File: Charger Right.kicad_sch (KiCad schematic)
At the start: 6 parts, among them Q3 AO4459, U2 CN3702

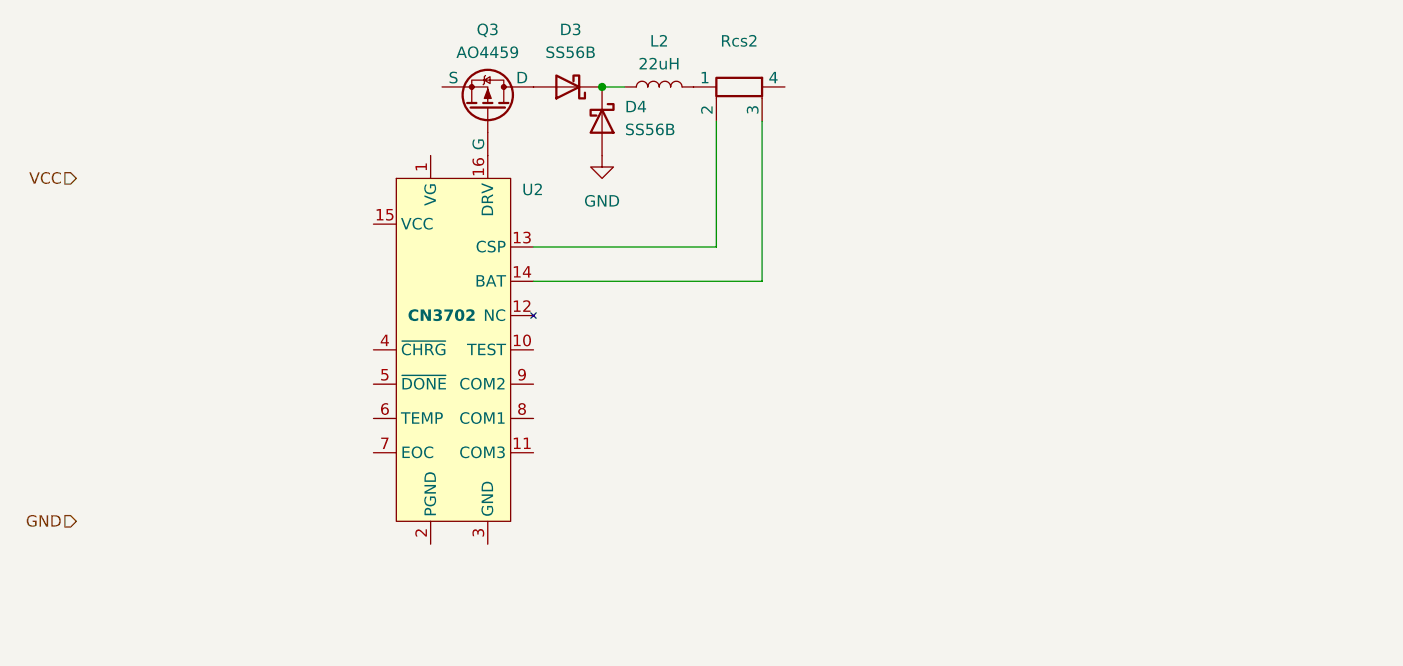
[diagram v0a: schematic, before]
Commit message: Add some resistors and caps
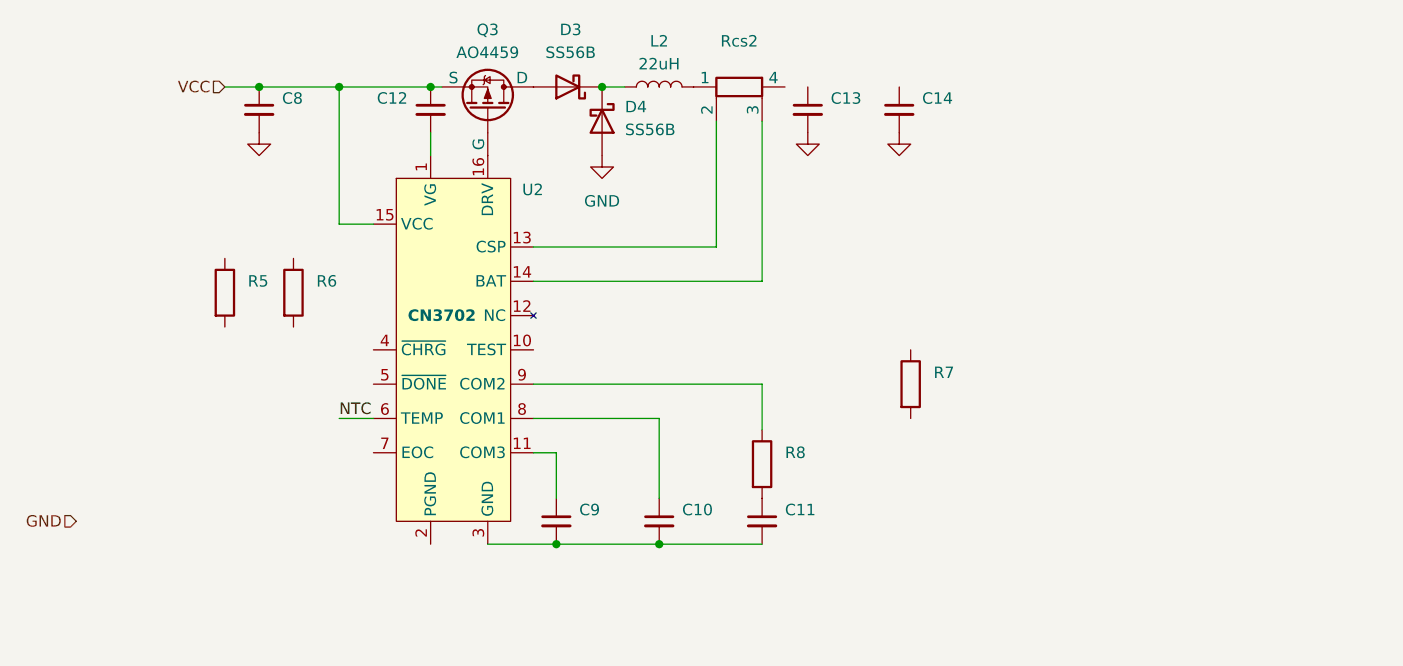
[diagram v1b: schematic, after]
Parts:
- added C10, C11, C12, C13, C14, C8, C9: (no value), symbol Device:C_Small
- added R5, R6, R7, R8: (no value), symbol Device:R
- Rcs2: footprint (none) -> BRAUNIT Charger:R_Shunt_2010_5025Metric
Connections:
- net GND: now also C13.2, C14.2, C8.2
- net VCC: now also Q3.1 (S), Q3.2 (S), Q3.3 (S), U2.15 (VCC), C12.1, C8.1
- net at U2.1 (VG): now also C12.2
- net at U2.11 (COM3): now also C9.1
- net at U2.3 (GND): now also C10.2, C11.2, C9.2
- net NTC: now reaches U2.6 (TEMP)
- net at U2.8 (COM1): now also C10.1
- net at U2.9 (COM2): now also R8.1
- new net: C11.1, R8.2

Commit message: Add BRAUNIT connector and battery detect/charge enable
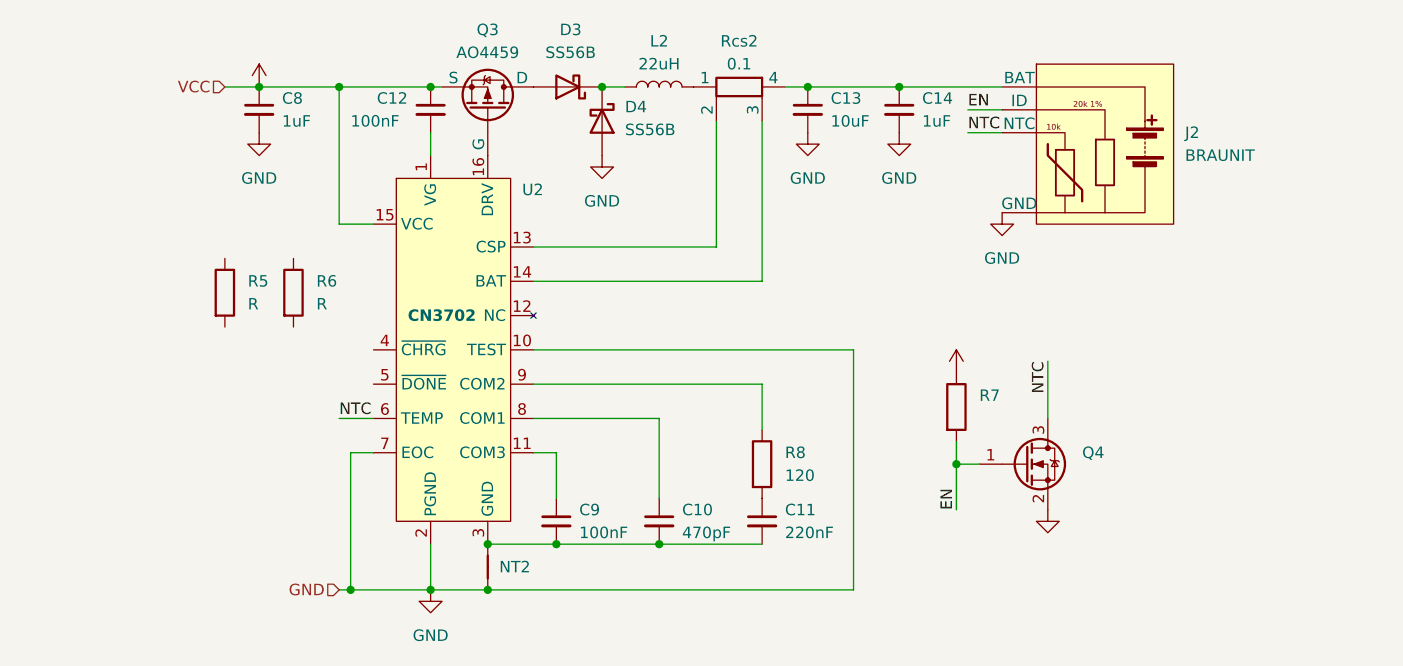
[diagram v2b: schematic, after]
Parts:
- added J2: BRAUNIT, BRAUNIT Charger:Blade_1x04_P2.5mm_Vertical_BRAUNIT_Loose, symbol BRAUNIT Charger:BRAUNIT
- added NT2: NetTie_2, NetTie:NetTie-2_SMD_Pad0.5mm, symbol Device:NetTie_2
- added Q4: (no value), symbol Transistor_FET:2N7002
- C10: value (none) -> 470pF; footprint (none) -> Capacitor_SMD:C_0805_2012Metric
- C11: value (none) -> 220nF; footprint (none) -> Capacitor_SMD:C_0805_2012Metric
- C12, C9: value (none) -> 100nF; footprint (none) -> Capacitor_SMD:C_0805_2012Metric
- C13: value (none) -> 10uF; footprint (none) -> Capacitor_SMD:C_1206_3216Metric
- C14, C8: value (none) -> 1uF; footprint (none) -> Capacitor_SMD:C_0805_2012Metric
- R5, R6: value (none) -> R
- R8: value (none) -> 120; footprint (none) -> Resistor_SMD:R_0805_2012Metric
- Rcs2: value (none) -> 0.1
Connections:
- net GND: now also U2.10 (TEST), U2.2 (PGND), U2.7 (EOC), J2.4 (GND), NT2.2, Q4.2 (S)
- net NTC: now also J2.3 (NTC), Q4.3 (D)
- net VCC: now also R7.1
- net at C10.2, C11.2, C9.2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: now also NT2.1
- net at C13.1: now also C14.1, Rcs2.4, J2.1 (BAT)
- net EN: now reaches R7.2
- net EN: now also J2.2 (ID), Q4.1 (G)
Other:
- moved on the sheet: R7

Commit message: Add LCSC part numbers for most components
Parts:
- removed D3, D4: SS56B, Diode_SMD:D_SMB, symbol BRAUNIT Charger:SS56B
- added D4, D5: (no value), symbol Device:D_Schottky
- added D6: LED_RAGB, symbol Device:LED_RAGB
- C10: value 470pF -> (none); footprint Capacitor_SMD:C_0805_2012Metric -> (none); LCSC (none) -> C107092
- C11: value 220nF -> (none); footprint Capacitor_SMD:C_0805_2012Metric -> (none); LCSC (none) -> C107131
- C12, C9: value 100nF -> (none); footprint Capacitor_SMD:C_0805_2012Metric -> (none); LCSC (none) -> C49678
- C13: value 10uF -> (none); footprint Capacitor_SMD:C_1206_3216Metric -> (none); LCSC (none) -> C109464
- C14, C8: value 1uF -> (none); footprint Capacitor_SMD:C_0805_2012Metric -> (none); LCSC (none) -> C91185
- J2: value BRAUNIT -> (none); footprint BRAUNIT Charger:Blade_1x04_P2.5mm_Vertical_BRAUNIT_Loose -> (none); now left out of the parts list
- L2: value 22uH -> (none); footprint Inductor_SMD:L_10.4x10.4_H4.8 -> (none); LCSC (none) -> C182173
- NT2: value NetTie_2 -> (none); footprint NetTie:NetTie-2_SMD_Pad0.5mm -> (none); now left out of the parts list
- Q3: value AO4459 -> (none); footprint Package_SO:SOIC-8_3.9x4.9mm_P1.27mm -> (none); LCSC (none) -> C49047
- Q4: LCSC (none) -> C8545
- R5: value R -> (none)
- R7: LCSC (none) -> C89104
- R8: value 120 -> (none); footprint Resistor_SMD:R_0805_2012Metric -> (none); LCSC (none) -> C114245
- Rcs2: value 0.1 -> (none); footprint BRAUNIT Charger:R_Shunt_2010_5025Metric -> (none); LCSC (none) -> C309644
- U2: value CN3702 -> (none); footprint Package_SO:TSSOP-16_4.4x5mm_P0.65mm -> (none); LCSC (none) -> C40655
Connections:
- net GND: now also D5.2 (A)
- net VCC: now also D6.2 (A)
- net at U2.4 (~{CHRG}): now also R5.2
- net at U2.5 (~{DONE}): now also R6.2
- net at L2.1: now also D4.1 (K), D5.1 (K)
- net at Q3.5 (D), Q3.6 (D), Q3.7 (D)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: now also D4.2 (A)
- net at R5.1: now also D6.1 (RK)
- net at R6.1: now also D6.3 (GK)
- no-connect marks 0 -> 1
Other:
- moved on the sheet: R5, R6

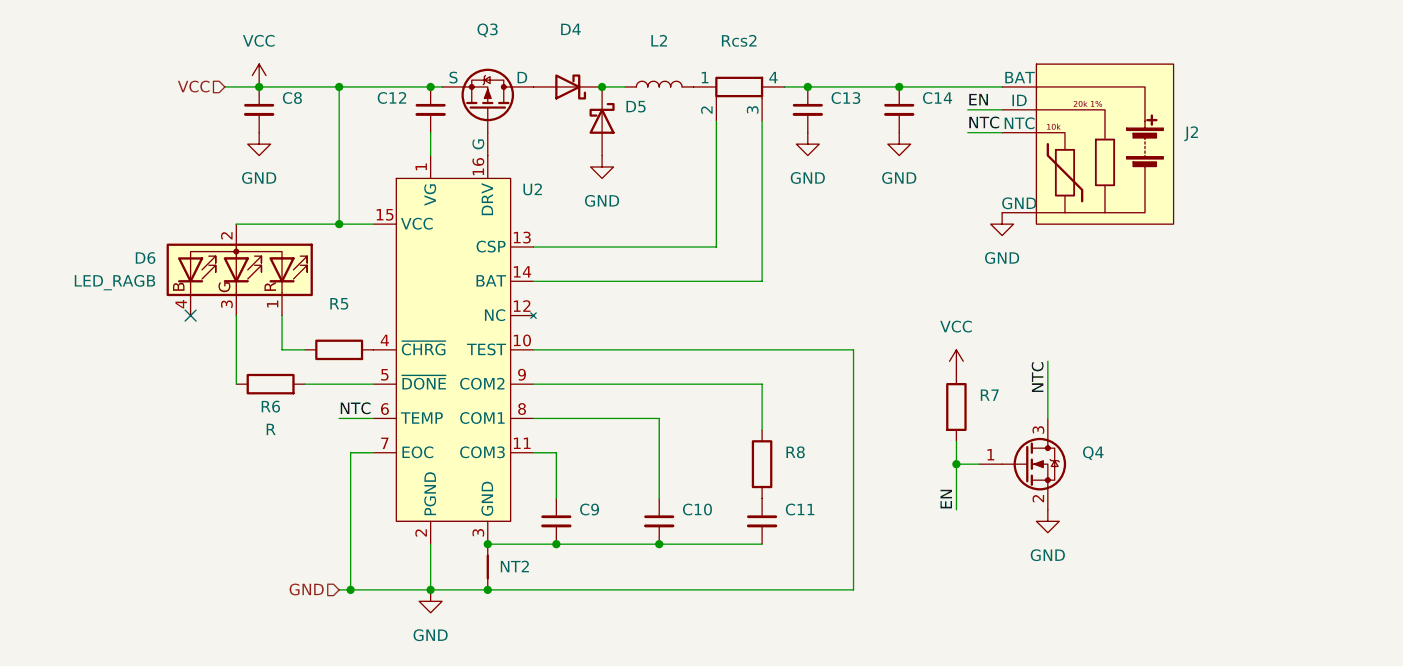
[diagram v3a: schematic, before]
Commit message: Add status indicator LED
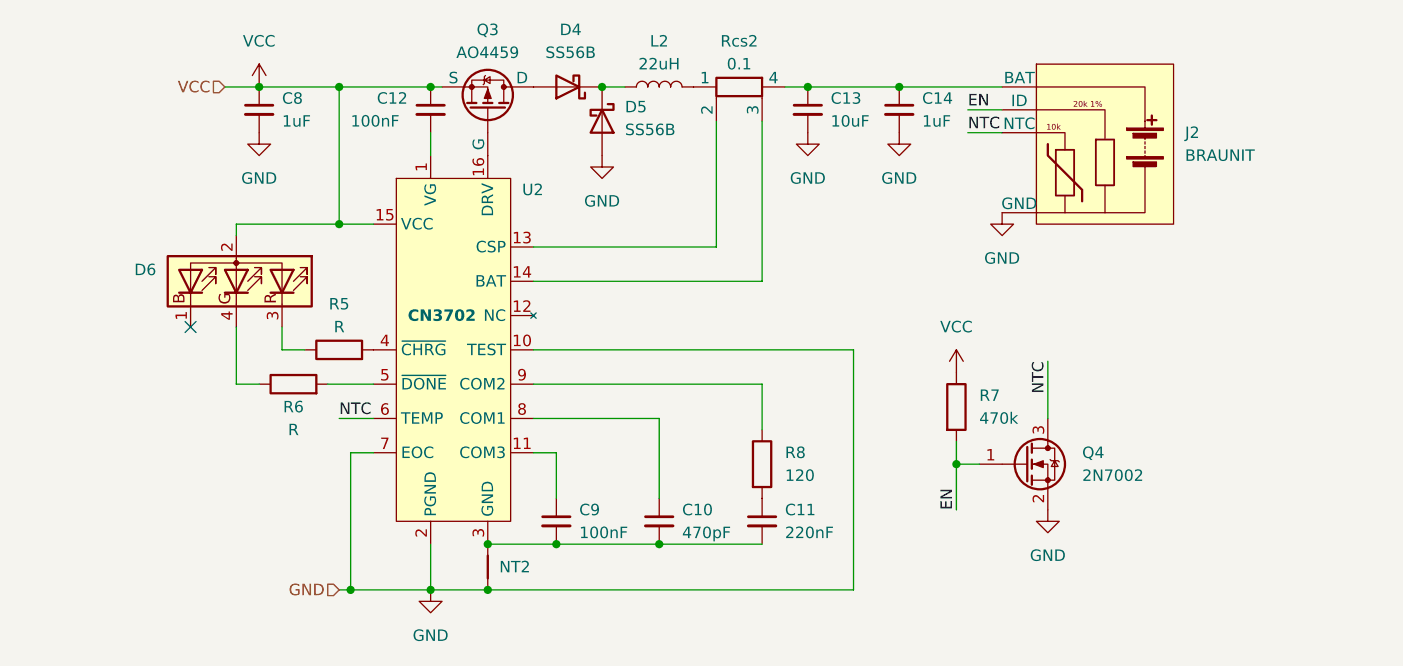
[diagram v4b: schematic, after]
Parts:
- removed D6: LED_RAGB, symbol Device:LED_RAGB
- added D6: (no value), symbol Device:LED_BARG
- C10: value (none) -> 470pF; footprint (none) -> Capacitor_SMD:C_0603_1608Metric
- C11: value (none) -> 220nF; footprint (none) -> Capacitor_SMD:C_0805_2012Metric
- C12, C9: value (none) -> 100nF; footprint (none) -> Capacitor_SMD:C_0805_2012Metric
- C13: value (none) -> 10uF; footprint (none) -> Capacitor_SMD:C_1206_3216Metric
- C14, C8: value (none) -> 1uF; footprint (none) -> Capacitor_SMD:C_0805_2012Metric
- D4, D5: value (none) -> SS56B; footprint (none) -> Diode_SMD:D_SMB
- J2: value (none) -> BRAUNIT; footprint (none) -> BRAUNIT Charger:Blade_1x04_P2.5mm_Vertical_BRAUNIT_Loose
- L2: value (none) -> 22uH; footprint (none) -> Inductor_SMD:L_10.4x10.4_H4.8
- NT2: value (none) -> NetTie_2; footprint (none) -> NetTie:NetTie-2_SMD_Pad0.5mm
- Q3: value (none) -> AO4459; footprint (none) -> Package_SO:SOIC-8_3.9x4.9mm_P1.27mm
- Q4: value (none) -> 2N7002; footprint (none) -> Package_TO_SOT_SMD:SOT-23
- R5: value (none) -> R
- R7: value (none) -> 470k; footprint (none) -> Resistor_SMD:R_0805_2012Metric
- R8: value (none) -> 120; footprint (none) -> Resistor_SMD:R_0805_2012Metric
- Rcs2: value (none) -> 0.1; footprint (none) -> BRAUNIT Charger:R_Shunt_2010_5025Metric
- U2: value (none) -> CN3702; footprint (none) -> Package_SO:TSSOP-16_4.4x5mm_P0.65mm
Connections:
- net VCC: now also D6.2 (A)
- net at R5.1: now also D6.3 (RK)
- net at R6.1: now also D6.4 (GK)
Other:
- moved on the sheet: R6

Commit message: Specify LED, resistors, and start on USB-C circuit
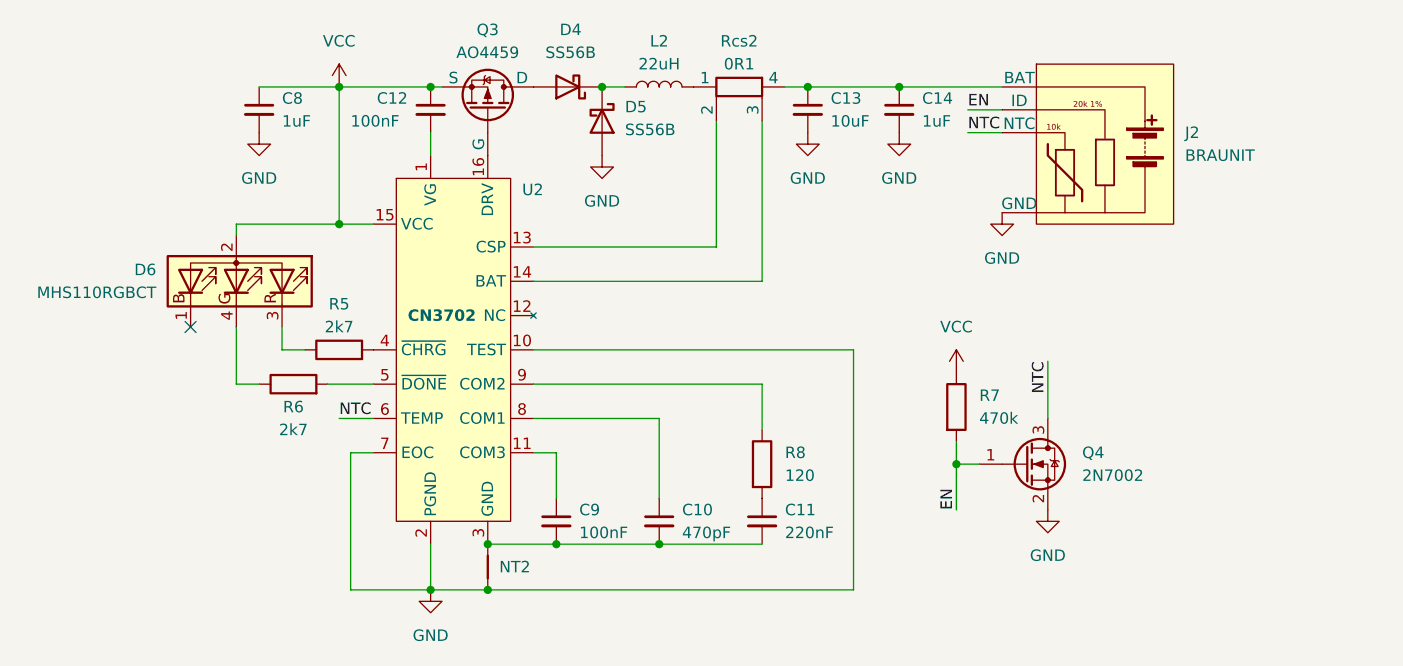
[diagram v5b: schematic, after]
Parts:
- D6: value (none) -> MHS110RGBCT; footprint (none) -> BRAUNIT Charger:LED_RGB_Meihua_MHS110RGBCT
- R5, R6: value R -> 2k7; footprint (none) -> Resistor_SMD:R_0603_1608Metric; LCSC (none) -> C114612
- Rcs2: value 0.1 -> 0R1
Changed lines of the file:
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@@
   (junction (at 138.43 123.19) (diameter 0) (color 0 0 0 0)
   )
-  (junction (at 115.57 128.27) (diameter 0) (color 0 0 0 0)
-  )
   (junction (at 114.3 72.39) (diameter 0) (color 0 0 0 0)
   )
@@
   )
   (junction (at 130.81 123.19) (diameter 0) (color 0 0 0 0)
-  )
-  (junction (at 105.41 72.39) (diameter 0) (color 0 0 0 0)
   )
   (junction (at 143.51 72.39) (diameter 0) (color 0 0 0 0)
@@
     (stroke (width 0) (type default) (color 0 0 0 0))
   )
-  (wire (pts (xy 101.6 72.39) (xy 105.41 72.39))
-    (stroke (width 0) (type default) (color 0 0 0 0))
-  )
   (wire (pts (xy 135.89 101.6) (xy 171.45 101.6))
     (stroke (width 0) (type default) (color 0 0 0 0))
@@
   )
   (wire (pts (xy 149.86 123.19) (xy 161.29 123.19))
-    (stroke (width 0) (type default) (color 0 0 0 0))
-  )
-  (wire (pts (xy 114.3 128.27) (xy 115.57 128.27))
     (stroke (width 0) (type default) (color 0 0 0 0))
   )
@@
   (label "NTC" (at 184.15 77.47 0)
     (effects (font (size 1.27 1.27)) (justify left bottom))
-  )
-  (hierarchical_label "VCC" (shape input) (at 101.6 72.39 180)
-    (effects (font (size 1.27 1.27)) (justify right))
-  )
-  (hierarchical_label "GND" (shape input) (at 114.3 128.27 180)
-    (effects (font (size 1.27 1.27)) (justify right))
   )
   (symbol (lib_id "power:GND") (at 143.51 80.01 0) (unit 1)
@@
     (pin "2")
   )
-  (symbol (lib_id "power:VCC") (at 105.41 72.39 0) (unit 1)
-    (in_bom yes) (on_board yes) (fields_autoplaced)
-    (property "Reference" "#PWR0118" (id 0) (at 105.41 76.2 0)
-      (effects (font (size 1.27 1.27)) hide)
-    )
-    (property "Value" "VCC" (id 1) (at 105.41 67.31 0))
-    (property "Footprint" "" (id 2) (at 105.41 72.39 0)
-      (effects (font (size 1.27 1.27)) hide)
-    )
-    (property "Datasheet" "" (id 3) (at 105.41 72.39 0)
+  (symbol (lib_id "power:VCC") (at 114.3 72.39 0) (unit 1)
+    (in_bom yes) (on_board yes) (fields_autoplaced)
+    (property "Reference" "#PWR0118" (id 0) (at 114.3 76.2 0)
+      (effects (font (size 1.27 1.27)) hide)
+    )
+    (property "Value" "VCC" (id 1) (at 114.3 67.31 0))
+    (property "Footprint" "" (id 2) (at 114.3 72.39 0)
+      (effects (font (size 1.27 1.27)) hide)
+    )
+    (property "Datasheet" "" (id 3) (at 114.3 72.39 0)
       (effects (font (size 1.27 1.27)) hide)
     )
@@
     (in_bom yes) (on_board yes)
     (property "Reference" "Rcs2" (id 0) (at 158.75 67.31 90))
-    (property "Value" "0.1" (id 1) (at 158.75 69.85 90))
+    (property "Value" "0R1" (id 1) (at 158.75 69.85 90))
     (property "Footprint" "BRAUNIT Charger:R_Shunt_2010_5025Metric" (id 2) (at 158.75 70.612 90)
       (effects (font (size 1.27 1.27)) hide)
@@
       (effects (font (size 1.27 1.27)) (justify right))
     )
-    (property "Value" "" (id 1) (at 93.98 95.25 90)
+    (property "Value" "MHS110RGBCT" (id 1) (at 93.98 95.25 90)
       (effects (font (size 1.27 1.27)) (justify right))
     )
-    (property "Footprint" "" (id 2) (at 101.6 93.98 0)
+    (property "Footprint" "BRAUNIT Charger:LED_RGB_Meihua_MHS110RGBCT" (id 2) (at 101.6 93.98 0)
       (effects (font (size 1.27 1.27)) hide)
     )
@@
     (in_bom yes) (on_board yes)
     (property "Reference" "R5" (id 0) (at 114.3 96.52 90))
-    (property "Value" "R" (id 1) (at 114.3 99.06 90))
-    (property "Footprint" "" (id 2) (at 114.3 103.378 90)
+    (property "Value" "2k7" (id 1) (at 114.3 99.06 90))
+    (property "Footprint" "Resistor_SMD:R_0603_1608Metric" (id 2) (at 114.3 103.378 90)
       (effects (font (size 1.27 1.27)) hide)
     )
     (property "Datasheet" "~" (id 3) (at 114.3 101.6 0)
+      (effects (font (size 1.27 1.27)) hide)
+    )
+    (property "LCSC" "C114612" (id 4) (at 114.3 101.6 90)
       (effects (font (size 1.27 1.27)) hide)
     )
@@
     (in_bom yes) (on_board yes)
     (property "Reference" "R6" (id 0) (at 109.22 107.95 90))
-    (property "Value" "R" (id 1) (at 109.22 110.49 90))
-    (property "Footprint" "" (id 2) (at 109.22 107.188 90)
+    (property "Value" "2k7" (id 1) (at 109.22 110.49 90))
+    (property "Footprint" "Resistor_SMD:R_0603_1608Metric" (id 2) (at 109.22 107.188 90)
       (effects (font (size 1.27 1.27)) hide)
     )
@@
       (effects (font (size 1.27 1.27)) hide)
     )
+    (property "LCSC" "C114612" (id 4) (at 109.22 105.41 90)
+      (effects (font (size 1.27 1.27)) hide)
+    )
